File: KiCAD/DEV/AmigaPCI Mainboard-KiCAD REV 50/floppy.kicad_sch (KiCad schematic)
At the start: 25 parts, among them CN203 DB25_Stack_FemaleAndMale, CN204 INTERNAL FLOPPY, J200 SHORT FOR DF1, J201 1-2 AMIGA DRIVES/2-3 PC DRIVES, J202 1-2 AMIGA DRIVES/2-3 PC DRIVES, J207 TICK, J208 TBASE, U204 8520, U209 74HCT08, U212 74HCT74, U213 74HCT00, U215 74HCT03, U219 74AHCT04, U305 74HCT08

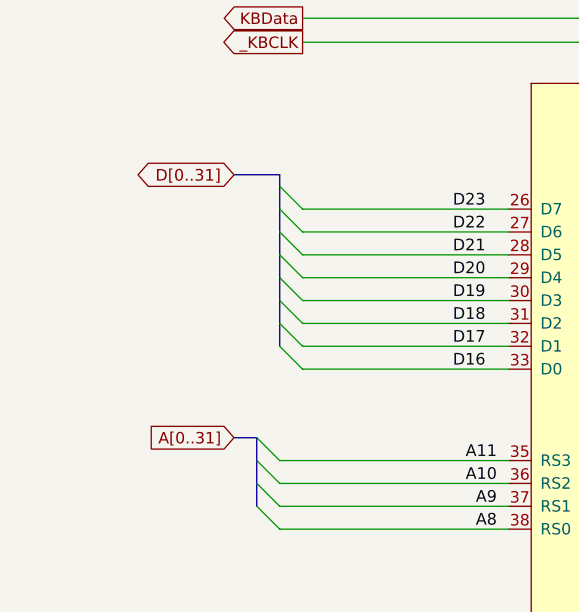
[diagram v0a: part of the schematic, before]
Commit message: Updated STM32F205 microcontroller.
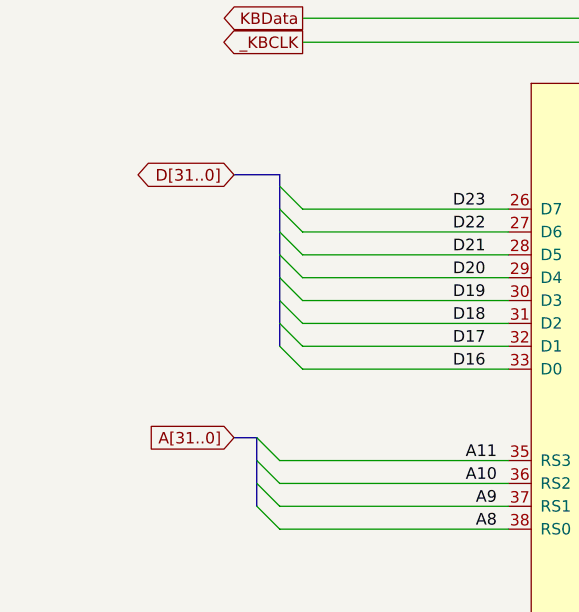
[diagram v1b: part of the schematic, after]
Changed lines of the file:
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@@
 		)
 	)
-	(global_label "A[0..31]"
+	(global_label "A[31..0]"
 		(shape input)
 		(at 37.846 96.266 180)
@@
 		)
 	)
-	(global_label "D[0..31]"
+	(global_label "D[31..0]"
 		(shape bidirectional)
 		(at 37.846 67.056 180)
